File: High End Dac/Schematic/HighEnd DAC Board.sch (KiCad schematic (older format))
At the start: 26 parts, among them CON1 CONN_01X13, P1 10K, P2 10K, U1 LT1012, U2 LT1012, U3 LTC2756, U4 LTC6655, U5 LM7805

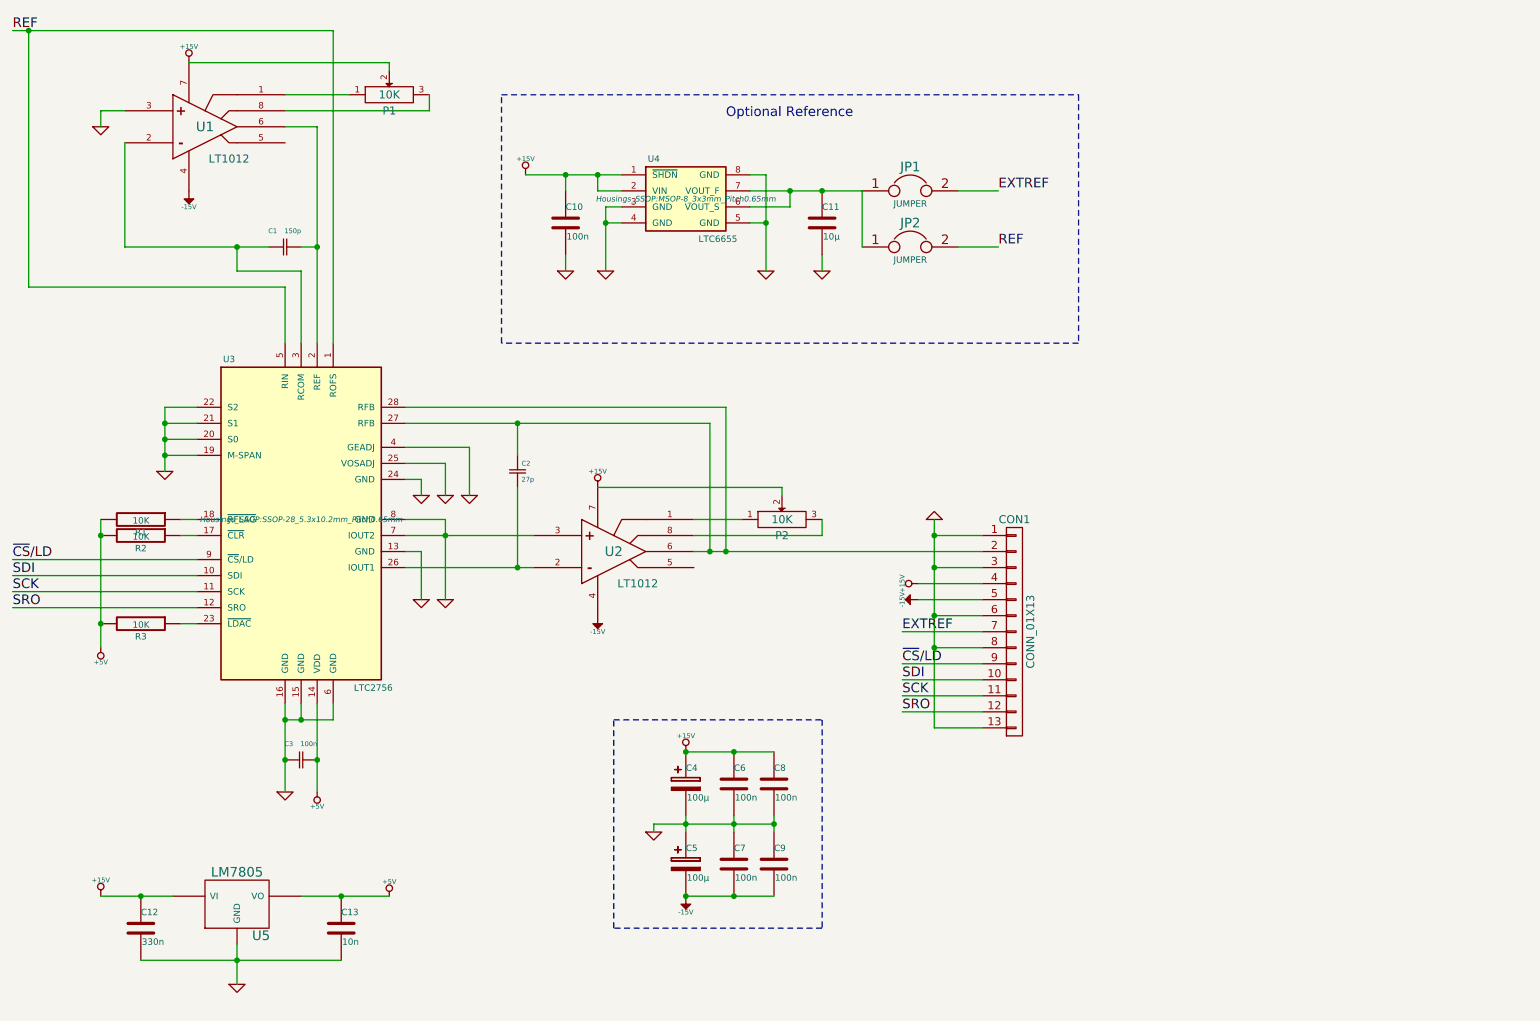
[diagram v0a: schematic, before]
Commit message: Added some PI Filter to the supply rails
Added some PI Filter to the supply rails
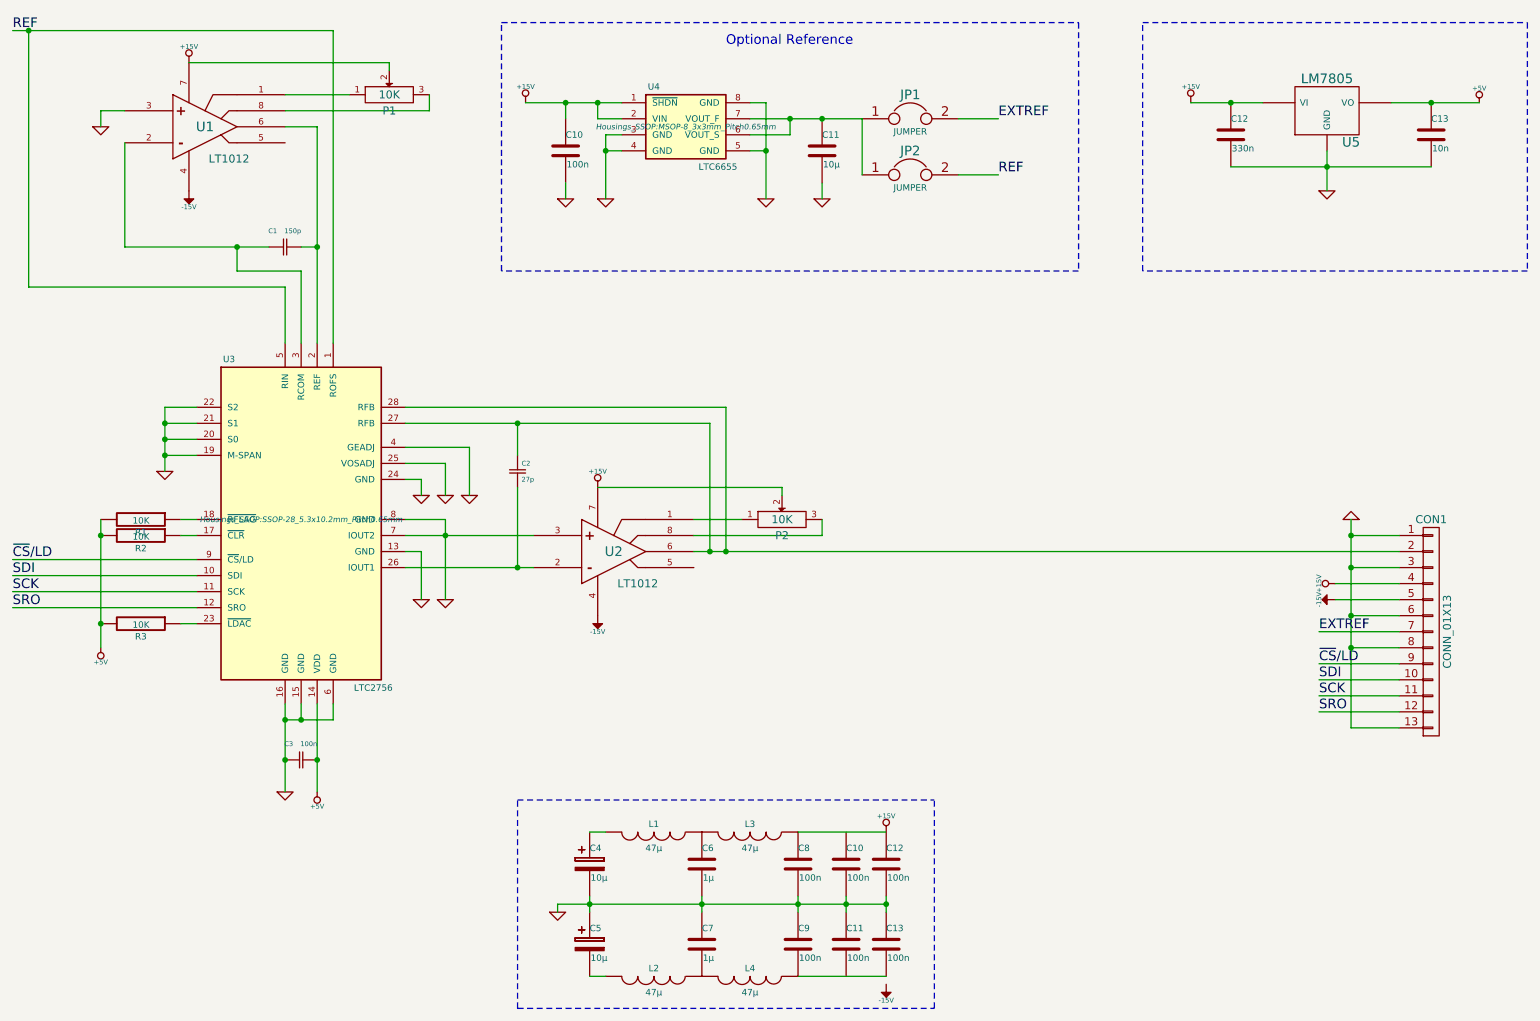
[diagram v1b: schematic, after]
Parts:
- added C12, C13: 100n, Capacitors_ThroughHole:C_Disc_D3_P2.5, symbol C
- added C6, C7: 1µ, Capacitors_ThroughHole:C_Disc_D3_P2.5, symbol C
- added L1, L2, L3, L4: 47µ, symbol INDUCTOR
- C4, C5: value 100µ -> 10µ
- renumbered C6 to C10, C7 to C11
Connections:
- net +15V: now also C12.1, L3.1; no longer C10.1, C4.1
- net -15V: no longer C11.2, C5.2, C9.2
- net GND: now also C12.2, C13.1, C6.2, C7.1
- new net: C4.1, L1.2
- new net: C5.2, L2.2
- new net: C13.2, C9.2, L4.1
- new net: C7.2, L2.1, L4.2
- new net: C6.1, L1.1, L3.2
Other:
- moved on the sheet: C10, C11, C12, C13, C4, C5, C8, C9, CON1, JP1, JP2, U4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
